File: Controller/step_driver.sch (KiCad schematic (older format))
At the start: 8 parts, among them CN2 CFG1, CN3 CFG1, CN4 CFG1, CN5 FEMALE_LEFT, CN6 FEMALE_RIGHT, J11 MotorTerm, J12 MotorHeader

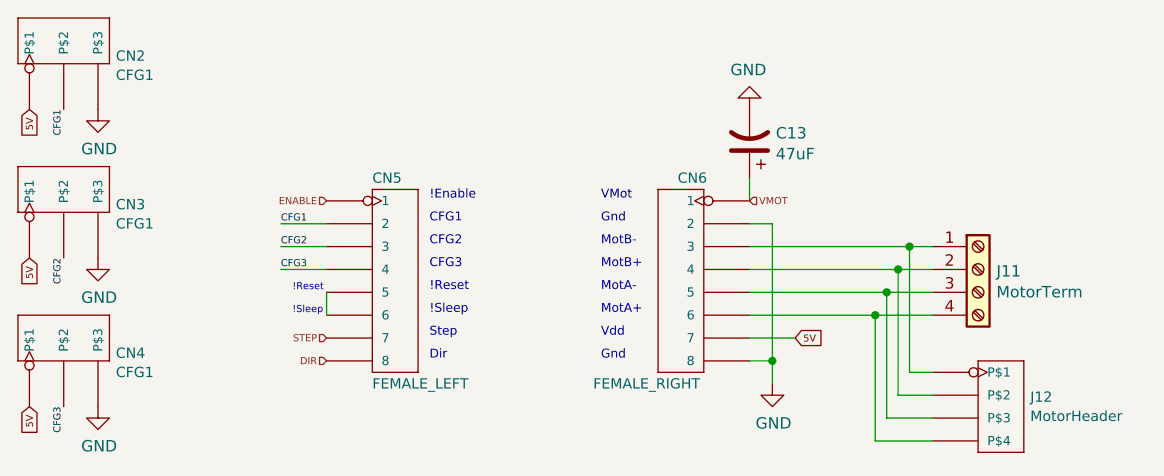
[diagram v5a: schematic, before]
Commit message: Creating Pi layout
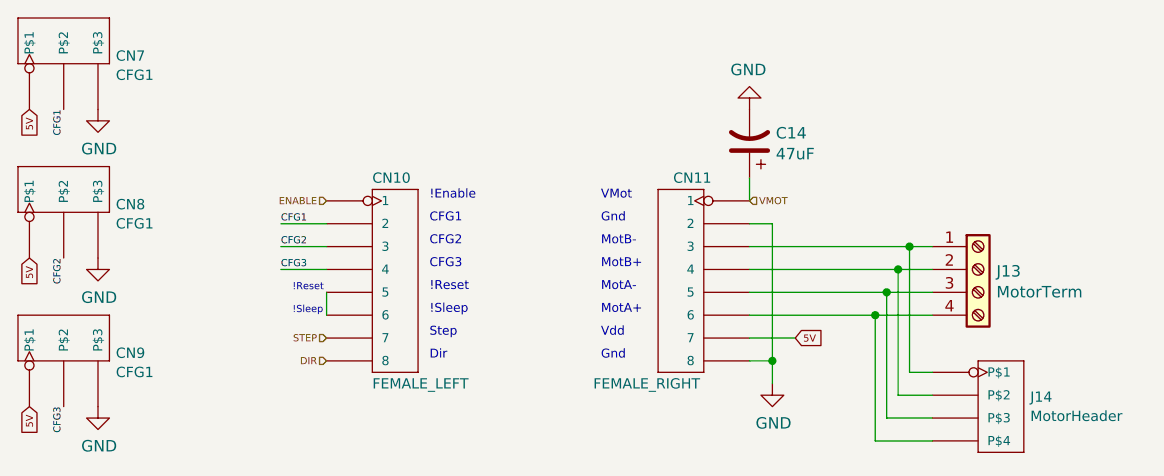
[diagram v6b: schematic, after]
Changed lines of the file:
@@
 $Descr A4 11693 8268
 encoding utf-8
-Sheet 3 4
+Sheet 4 4
 Title ""
 Date ""
@@
 AR Path="/5D4C0FEF/5D4B02F5" Ref="CN?"  Part="1"
 AR Path="/5D4C1080/5D4B02F5" Ref="CN10"  Part="1"
-F 0 "CN5" H 4000 3350 45  0000 L CNN
+F 0 "CN10" H 4000 3350 45  0000 L CNN
 F 1 "FEMALE_LEFT" H 4000 2450 45  0000 L CNN
 F 2 "OPL_Connector:H8-2.54" H 4100 2900 50  0001 C CNN
@@
 AR Path="/5D4C0FEF/5D4B13AD" Ref="CN?"  Part="1"
 AR Path="/5D4C1080/5D4B13AD" Ref="CN11"  Part="1"
-F 0 "CN6" H 5300 3350 45  0000 C CNN
+F 0 "CN11" H 5300 3350 45  0000 C CNN
 F 1 "FEMALE_RIGHT" H 5500 2450 45  0000 C CNN
 F 2 "OPL_Connector:H8-2.54" H 5350 2900 50  0001 C CNN
@@
 AR Path="/5D4C0FEF/5D4B27F8" Ref="C?"  Part="1"
 AR Path="/5D4C1080/5D4B27F8" Ref="C14"  Part="1"
-F 0 "C13" H 5535 2254 50  0000 R CNN
+F 0 "C14" H 5535 2254 50  0000 R CNN
 F 1 "47uF" H 5535 2345 50  0000 R CNN
 F 2 "Capacitor_SMD:CP_Elec_6.3x5.4" H 5650 2300 50  0001 C CNN
@@
 AR Path="/5D4C0FEF/5D4BDC37" Ref="CN?"  Part="1"
 AR Path="/5D4C1080/5D4BDC37" Ref="CN8"  Part="1"
-F 0 "CN3" V 2584 2272 45  0000 R CNN
+F 0 "CN8" V 2584 2272 45  0000 R CNN
 F 1 "CFG1" V 2500 2272 45  0000 R CNN
 F 2 "OPL_Connector:H3-2.54" H 2650 2500 50  0001 C CNN
@@
 AR Path="/5D4C0FEF/5D4BEA96" Ref="CN?"  Part="1"
 AR Path="/5D4C1080/5D4BEA96" Ref="CN9"  Part="1"
-F 0 "CN4" V 2584 2922 45  0000 R CNN
+F 0 "CN9" V 2584 2922 45  0000 R CNN
 F 1 "CFG1" V 2500 2922 45  0000 R CNN
 F 2 "OPL_Connector:H3-2.54" H 2650 3150 50  0001 C CNN
@@
 AR Path="/5D4C0FEF/5D4BBA78" Ref="CN?"  Part="1"
 AR Path="/5D4C1080/5D4BBA78" Ref="CN7"  Part="1"
-F 0 "CN2" V 2584 1622 45  0000 R CNN
+F 0 "CN7" V 2584 1622 45  0000 R CNN
 F 1 "CFG1" V 2500 1622 45  0000 R CNN
 F 2 "OPL_Connector:H3-2.54" H 2650 1850 50  0001 C CNN
@@
 AR Path="/5D4AFE00/5D4D9DAD" Ref="J11"  Part="1"
 AR Path="/5D4C1080/5D4D9DAD" Ref="J13"  Part="1"
-F 0 "J11" H 6730 2842 50  0000 L CNN
+F 0 "J13" H 6730 2842 50  0000 L CNN
 F 1 "MotorTerm" H 6730 2751 50  0000 L CNN
 F 2 "TerminalBlock_Phoenix:TerminalBlock_Phoenix_MPT-0,5-4-2.54_1x04_P2.54mm_Horizontal" H 6650 2850 50  0001 C CNN
@@
 AR Path="/5D4AFE00/5D567ECA" Ref="J12"  Part="1"
 AR Path="/5D4C1080/5D567ECA" Ref="J14"  Part="1"
-F 0 "J12" H 6878 3492 45  0000 L CNN
+F 0 "J14" H 6878 3492 45  0000 L CNN
 F 1 "MotorHeader" H 6878 3408 45  0000 L CNN
 F 2 "OPL_Connector:H4-2.54" H 6750 3450 50  0001 C CNN

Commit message: Probably giving up on Pi option
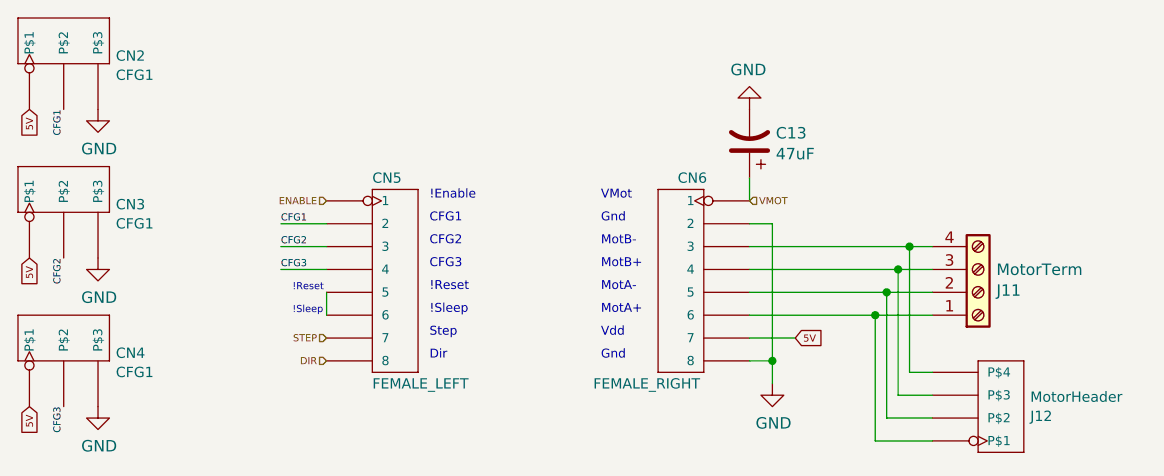
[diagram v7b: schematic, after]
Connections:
- net at J11.1 (Pin_1), J12.1 (P$1): now also CN6.6; no longer CN6.3
- net at J11.2 (Pin_2), J12.2 (P$2): now also CN6.5; no longer CN6.4
- net at J11.3 (Pin_3), J12.3 (P$3): now also CN6.4; no longer CN6.5
- net at J11.4 (Pin_4), J12.4 (P$4): now also CN6.3; no longer CN6.6
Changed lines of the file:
@@
 $Descr A4 11693 8268
 encoding utf-8
-Sheet 4 4
+Sheet 3 4
 Title ""
 Date ""
@@
 AR Path="/5D4C0FEF/5D4B02F5" Ref="CN?"  Part="1"
 AR Path="/5D4C1080/5D4B02F5" Ref="CN10"  Part="1"
-F 0 "CN10" H 4000 3350 45  0000 L CNN
+F 0 "CN5" H 4000 3350 45  0000 L CNN
 F 1 "FEMALE_LEFT" H 4000 2450 45  0000 L CNN
 F 2 "OPL_Connector:H8-2.54" H 4100 2900 50  0001 C CNN
@@
 AR Path="/5D4C0FEF/5D4B13AD" Ref="CN?"  Part="1"
 AR Path="/5D4C1080/5D4B13AD" Ref="CN11"  Part="1"
-F 0 "CN11" H 5300 3350 45  0000 C CNN
+F 0 "CN6" H 5300 3350 45  0000 C CNN
 F 1 "FEMALE_RIGHT" H 5500 2450 45  0000 C CNN
 F 2 "OPL_Connector:H8-2.54" H 5350 2900 50  0001 C CNN
@@
 AR Path="/5D4C0FEF/5D4B27F8" Ref="C?"  Part="1"
 AR Path="/5D4C1080/5D4B27F8" Ref="C14"  Part="1"
-F 0 "C14" H 5535 2254 50  0000 R CNN
+F 0 "C13" H 5535 2254 50  0000 R CNN
 F 1 "47uF" H 5535 2345 50  0000 R CNN
 F 2 "Capacitor_SMD:CP_Elec_6.3x5.4" H 5650 2300 50  0001 C CNN
@@
 AR Path="/5D4C0FEF/5D4B699E" Ref="#PWR?"  Part="1"
 AR Path="/5D4C1080/5D4B699E" Ref="#PWR031"  Part="1"
-F 0 "#PWR031" H 5650 1900 50  0001 C CNN
+F 0 "#PWR026" H 5650 1900 50  0001 C CNN
 F 1 "GND" H 5655 1977 50  0000 C CNN
 F 2 "" H 5650 2150 50  0001 C CNN
@@
 AR Path="/5D4C0FEF/5D4B88E4" Ref="#PWR?"  Part="1"
 AR Path="/5D4C1080/5D4B88E4" Ref="#PWR032"  Part="1"
-F 0 "#PWR032" H 5750 3100 50  0001 C CNN
+F 0 "#PWR027" H 5750 3100 50  0001 C CNN
 F 1 "GND" H 5755 3177 50  0000 C CNN
 F 2 "" H 5750 3350 50  0001 C CNN
@@
 AR Path="/5D4C0FEF/5D4BCF63" Ref="#PWR?"  Part="1"
 AR Path="/5D4C1080/5D4BCF63" Ref="#PWR028"  Part="1"
-F 0 "#PWR028" H 2800 1900 50  0001 C CNN
+F 0 "#PWR023" H 2800 1900 50  0001 C CNN
 F 1 "GND" H 2805 1977 50  0000 C CNN
 F 2 "" H 2800 2150 50  0001 C CNN
@@
 AR Path="/5D4C0FEF/5D4BDC37" Ref="CN?"  Part="1"
 AR Path="/5D4C1080/5D4BDC37" Ref="CN8"  Part="1"
-F 0 "CN8" V 2584 2272 45  0000 R CNN
+F 0 "CN3" V 2584 2272 45  0000 R CNN
 F 1 "CFG1" V 2500 2272 45  0000 R CNN
 F 2 "OPL_Connector:H3-2.54" H 2650 2500 50  0001 C CNN
@@
 AR Path="/5D4C0FEF/5D4BDC43" Ref="#PWR?"  Part="1"
 AR Path="/5D4C1080/5D4BDC43" Ref="#PWR029"  Part="1"
-F 0 "#PWR029" H 2800 2550 50  0001 C CNN
+F 0 "#PWR024" H 2800 2550 50  0001 C CNN
 F 1 "GND" H 2805 2627 50  0000 C CNN
 F 2 "" H 2800 2800 50  0001 C CNN
@@
 AR Path="/5D4C0FEF/5D4BEA96" Ref="CN?"  Part="1"
 AR Path="/5D4C1080/5D4BEA96" Ref="CN9"  Part="1"
-F 0 "CN9" V 2584 2922 45  0000 R CNN
+F 0 "CN4" V 2584 2922 45  0000 R CNN
 F 1 "CFG1" V 2500 2922 45  0000 R CNN
 F 2 "OPL_Connector:H3-2.54" H 2650 3150 50  0001 C CNN
@@
 AR Path="/5D4C0FEF/5D4BEAA2" Ref="#PWR?"  Part="1"
 AR Path="/5D4C1080/5D4BEAA2" Ref="#PWR030"  Part="1"
-F 0 "#PWR030" H 2800 3200 50  0001 C CNN
+F 0 "#PWR025" H 2800 3200 50  0001 C CNN
 F 1 "GND" H 2805 3277 50  0000 C CNN
 F 2 "" H 2800 3450 50  0001 C CNN
@@
 AR Path="/5D4C0FEF/5D4BBA78" Ref="CN?"  Part="1"
 AR Path="/5D4C1080/5D4BBA78" Ref="CN7"  Part="1"
-F 0 "CN7" V 2584 1622 45  0000 R CNN
+F 0 "CN2" V 2584 1622 45  0000 R CNN
 F 1 "CFG1" V 2500 1622 45  0000 R CNN
 F 2 "OPL_Connector:H3-2.54" H 2650 1850 50  0001 C CNN
@@
 L Connector:Screw_Terminal_01x04 J?
 U 1 1 5D4D9DAD
-P 6650 2850
+P 6650 2950
 AR Path="/5D4D9DAD" Ref="J?"  Part="1"
 AR Path="/5D4AFE00/5D4D9DAD" Ref="J11"  Part="1"
 AR Path="/5D4C1080/5D4D9DAD" Ref="J13"  Part="1"
-F 0 "J13" H 6730 2842 50  0000 L CNN
-F 1 "MotorTerm" H 6730 2751 50  0000 L CNN
-F 2 "TerminalBlock_Phoenix:TerminalBlock_Phoenix_MPT-0,5-4-2.54_1x04_P2.54mm_Horizontal" H 6650 2850 50  0001 C CNN
-F 3 "~" H 6650 2850 50  0001 C CNN
-F 4 "320110143" H 6650 2850 50  0001 C CNN "SKU"
-F 5 "GS019-2.54-04P-5" H 6650 2850 50  0001 C CNN "MPN"
-	1    6650 2850
-	1    0    0    -1
+F 0 "J11" H 6730 2942 50  0000 L CNN
+F 1 "MotorTerm" H 6730 2851 50  0000 L CNN
+F 2 "TerminalBlock_Phoenix:TerminalBlock_Phoenix_MPT-0,5-4-2.54_1x04_P2.54mm_Horizontal" H 6650 2950 50  0001 C CNN
+F 3 "~" H 6650 2950 50  0001 C CNN
+F 4 "320110143" H 6650 2950 50  0001 C CNN "SKU"
+F 5 "GS019-2.54-04P-5" H 6650 2950 50  0001 C CNN "MPN"
+	1    6650 2950
+	1    0    0    1
 $EndComp
 $Comp
@@
 AR Path="/5D4AFE00/5D567ECA" Ref="J12"  Part="1"
 AR Path="/5D4C1080/5D567ECA" Ref="J14"  Part="1"
-F 0 "J14" H 6878 3492 45  0000 L CNN
+F 0 "J12" H 6878 3492 45  0000 L CNN
 F 1 "MotorHeader" H 6878 3408 45  0000 L CNN
 F 2 "OPL_Connector:H4-2.54" H 6750 3450 50  0001 C CNN
@@
 F 5 "320020017" H 6780 3600 20  0001 C CNN "SKU"
 	1    6750 3450
-	1    0    0    -1
-$EndComp
-Wire Wire Line
+	1    0    0    1
+$EndComp
+Wire Wire Line

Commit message: Mostly final layout
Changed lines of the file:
@@
 $Descr A4 11693 8268
 encoding utf-8
-Sheet 3 4
+Sheet 4 4
 Title ""
 Date ""
@@
 AR Path="/5D4C0FEF/5D4B02F5" Ref="CN?"  Part="1"
 AR Path="/5D4C1080/5D4B02F5" Ref="CN10"  Part="1"
-F 0 "CN5" H 4000 3350 45  0000 L CNN
+F 0 "CN10" H 4000 3350 45  0000 L CNN
 F 1 "FEMALE_LEFT" H 4000 2450 45  0000 L CNN
 F 2 "OPL_Connector:H8-2.54" H 4100 2900 50  0001 C CNN
@@
 AR Path="/5D4C0FEF/5D4B13AD" Ref="CN?"  Part="1"
 AR Path="/5D4C1080/5D4B13AD" Ref="CN11"  Part="1"
-F 0 "CN6" H 5300 3350 45  0000 C CNN
+F 0 "CN11" H 5300 3350 45  0000 C CNN
 F 1 "FEMALE_RIGHT" H 5500 2450 45  0000 C CNN
 F 2 "OPL_Connector:H8-2.54" H 5350 2900 50  0001 C CNN
@@
 AR Path="/5D4C0FEF/5D4B27F8" Ref="C?"  Part="1"
 AR Path="/5D4C1080/5D4B27F8" Ref="C14"  Part="1"
-F 0 "C13" H 5535 2254 50  0000 R CNN
+F 0 "C14" H 5535 2254 50  0000 R CNN
 F 1 "47uF" H 5535 2345 50  0000 R CNN
 F 2 "Capacitor_SMD:CP_Elec_6.3x5.4" H 5650 2300 50  0001 C CNN
@@
 AR Path="/5D4C0FEF/5D4B699E" Ref="#PWR?"  Part="1"
 AR Path="/5D4C1080/5D4B699E" Ref="#PWR031"  Part="1"
-F 0 "#PWR026" H 5650 1900 50  0001 C CNN
+F 0 "#PWR031" H 5650 1900 50  0001 C CNN
 F 1 "GND" H 5655 1977 50  0000 C CNN
 F 2 "" H 5650 2150 50  0001 C CNN
@@
 AR Path="/5D4C0FEF/5D4B88E4" Ref="#PWR?"  Part="1"
 AR Path="/5D4C1080/5D4B88E4" Ref="#PWR032"  Part="1"
-F 0 "#PWR027" H 5750 3100 50  0001 C CNN
+F 0 "#PWR032" H 5750 3100 50  0001 C CNN
 F 1 "GND" H 5755 3177 50  0000 C CNN
 F 2 "" H 5750 3350 50  0001 C CNN
@@
 AR Path="/5D4C0FEF/5D4BCF63" Ref="#PWR?"  Part="1"
 AR Path="/5D4C1080/5D4BCF63" Ref="#PWR028"  Part="1"
-F 0 "#PWR023" H 2800 1900 50  0001 C CNN
+F 0 "#PWR028" H 2800 1900 50  0001 C CNN
 F 1 "GND" H 2805 1977 50  0000 C CNN
 F 2 "" H 2800 2150 50  0001 C CNN
@@
 AR Path="/5D4C0FEF/5D4BDC37" Ref="CN?"  Part="1"
 AR Path="/5D4C1080/5D4BDC37" Ref="CN8"  Part="1"
-F 0 "CN3" V 2584 2272 45  0000 R CNN
+F 0 "CN8" V 2584 2272 45  0000 R CNN
 F 1 "CFG1" V 2500 2272 45  0000 R CNN
 F 2 "OPL_Connector:H3-2.54" H 2650 2500 50  0001 C CNN
@@
 AR Path="/5D4C0FEF/5D4BDC43" Ref="#PWR?"  Part="1"
 AR Path="/5D4C1080/5D4BDC43" Ref="#PWR029"  Part="1"
-F 0 "#PWR024" H 2800 2550 50  0001 C CNN
+F 0 "#PWR029" H 2800 2550 50  0001 C CNN
 F 1 "GND" H 2805 2627 50  0000 C CNN
 F 2 "" H 2800 2800 50  0001 C CNN
@@
 AR Path="/5D4C0FEF/5D4BEA96" Ref="CN?"  Part="1"
 AR Path="/5D4C1080/5D4BEA96" Ref="CN9"  Part="1"
-F 0 "CN4" V 2584 2922 45  0000 R CNN
+F 0 "CN9" V 2584 2922 45  0000 R CNN
 F 1 "CFG1" V 2500 2922 45  0000 R CNN
 F 2 "OPL_Connector:H3-2.54" H 2650 3150 50  0001 C CNN
@@
 AR Path="/5D4C0FEF/5D4BEAA2" Ref="#PWR?"  Part="1"
 AR Path="/5D4C1080/5D4BEAA2" Ref="#PWR030"  Part="1"
-F 0 "#PWR025" H 2800 3200 50  0001 C CNN
+F 0 "#PWR030" H 2800 3200 50  0001 C CNN
 F 1 "GND" H 2805 3277 50  0000 C CNN
 F 2 "" H 2800 3450 50  0001 C CNN
@@
 AR Path="/5D4C0FEF/5D4BBA78" Ref="CN?"  Part="1"
 AR Path="/5D4C1080/5D4BBA78" Ref="CN7"  Part="1"
-F 0 "CN2" V 2584 1622 45  0000 R CNN
+F 0 "CN7" V 2584 1622 45  0000 R CNN
 F 1 "CFG1" V 2500 1622 45  0000 R CNN
 F 2 "OPL_Connector:H3-2.54" H 2650 1850 50  0001 C CNN
@@
 AR Path="/5D4AFE00/5D4D9DAD" Ref="J11"  Part="1"
 AR Path="/5D4C1080/5D4D9DAD" Ref="J13"  Part="1"
-F 0 "J11" H 6730 2942 50  0000 L CNN
+F 0 "J13" H 6730 2942 50  0000 L CNN
 F 1 "MotorTerm" H 6730 2851 50  0000 L CNN
 F 2 "TerminalBlock_Phoenix:TerminalBlock_Phoenix_MPT-0,5-4-2.54_1x04_P2.54mm_Horizontal" H 6650 2950 50  0001 C CNN
@@
 AR Path="/5D4AFE00/5D567ECA" Ref="J12"  Part="1"
 AR Path="/5D4C1080/5D567ECA" Ref="J14"  Part="1"
-F 0 "J12" H 6878 3492 45  0000 L CNN
+F 0 "J14" H 6878 3492 45  0000 L CNN
 F 1 "MotorHeader" H 6878 3408 45  0000 L CNN
 F 2 "OPL_Connector:H4-2.54" H 6750 3450 50  0001 C CNN
